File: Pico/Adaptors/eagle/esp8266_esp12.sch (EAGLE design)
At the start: 15 parts, among them J1 JST-2P-SMD-PW-3410050P1

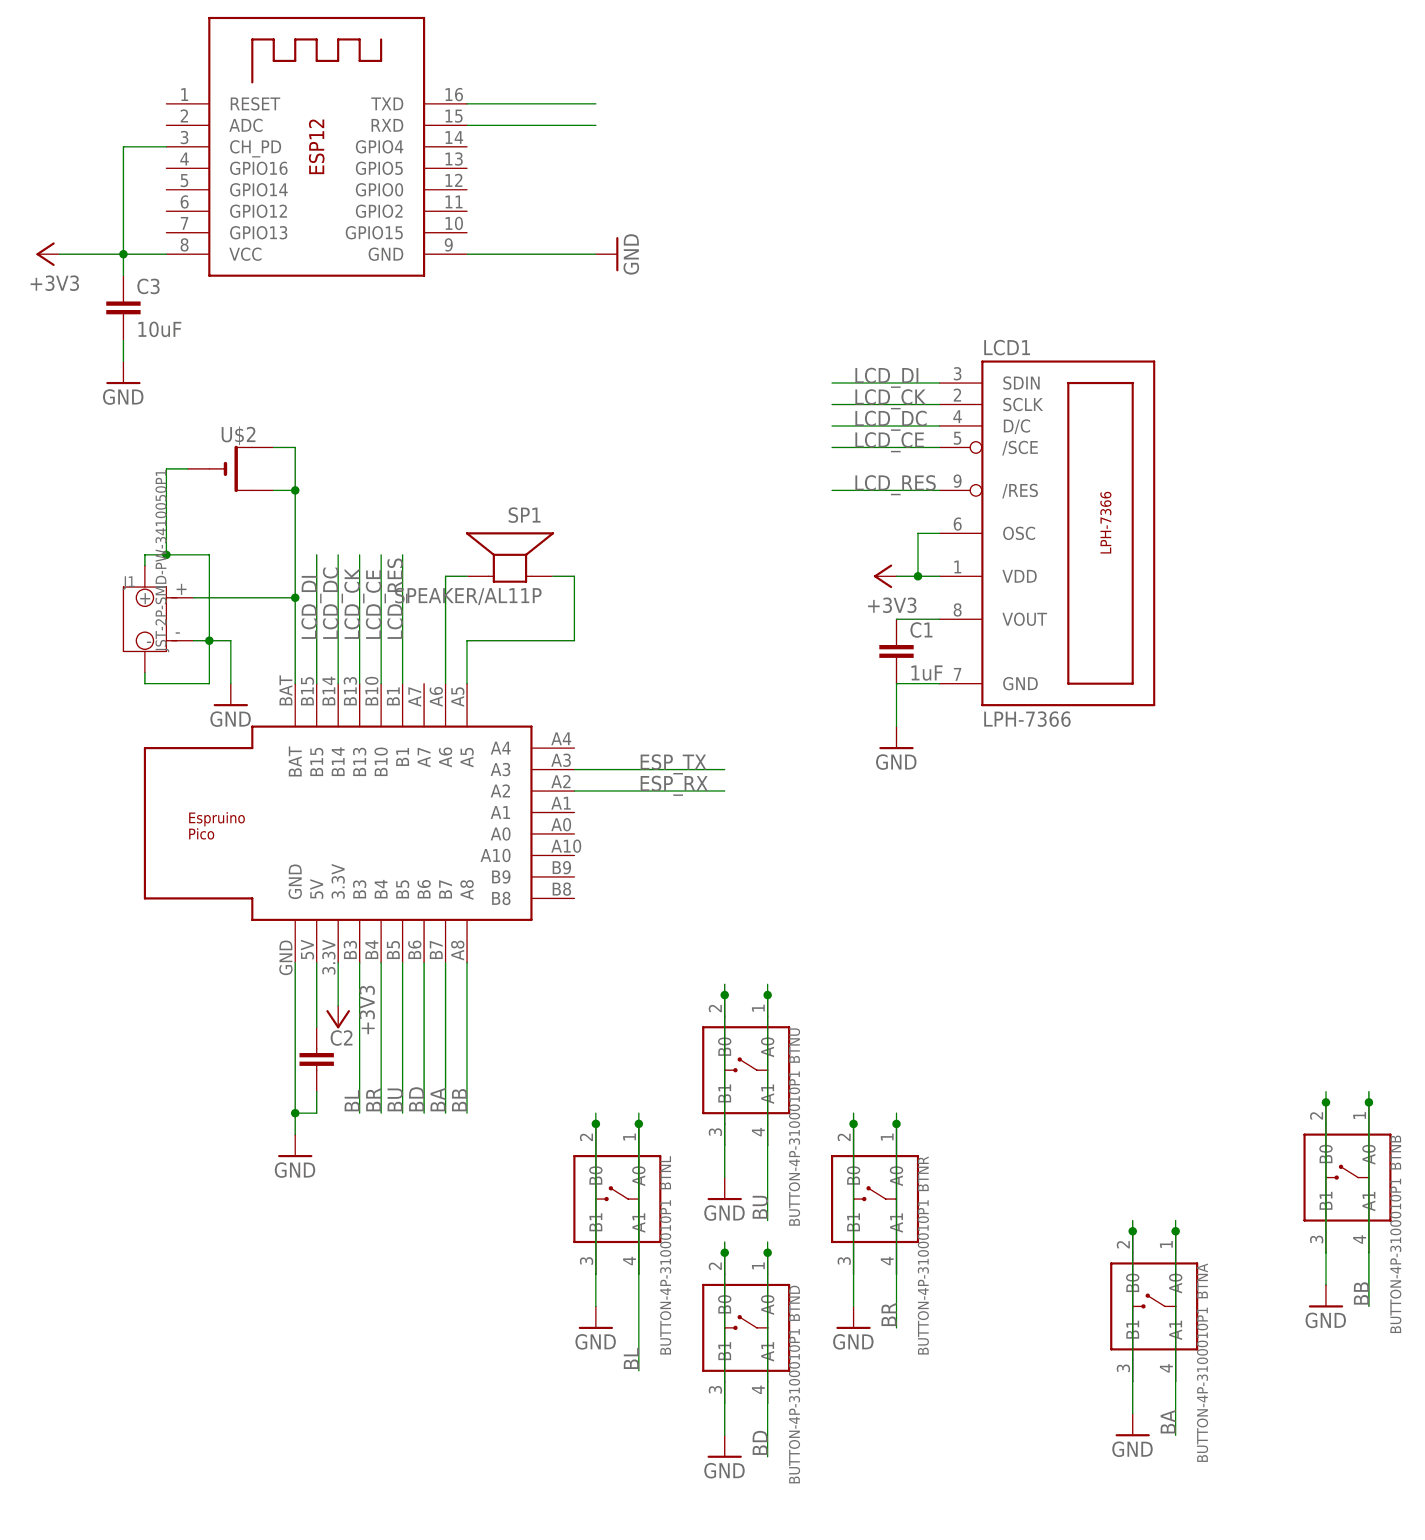
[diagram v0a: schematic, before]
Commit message: added ESP12 shim
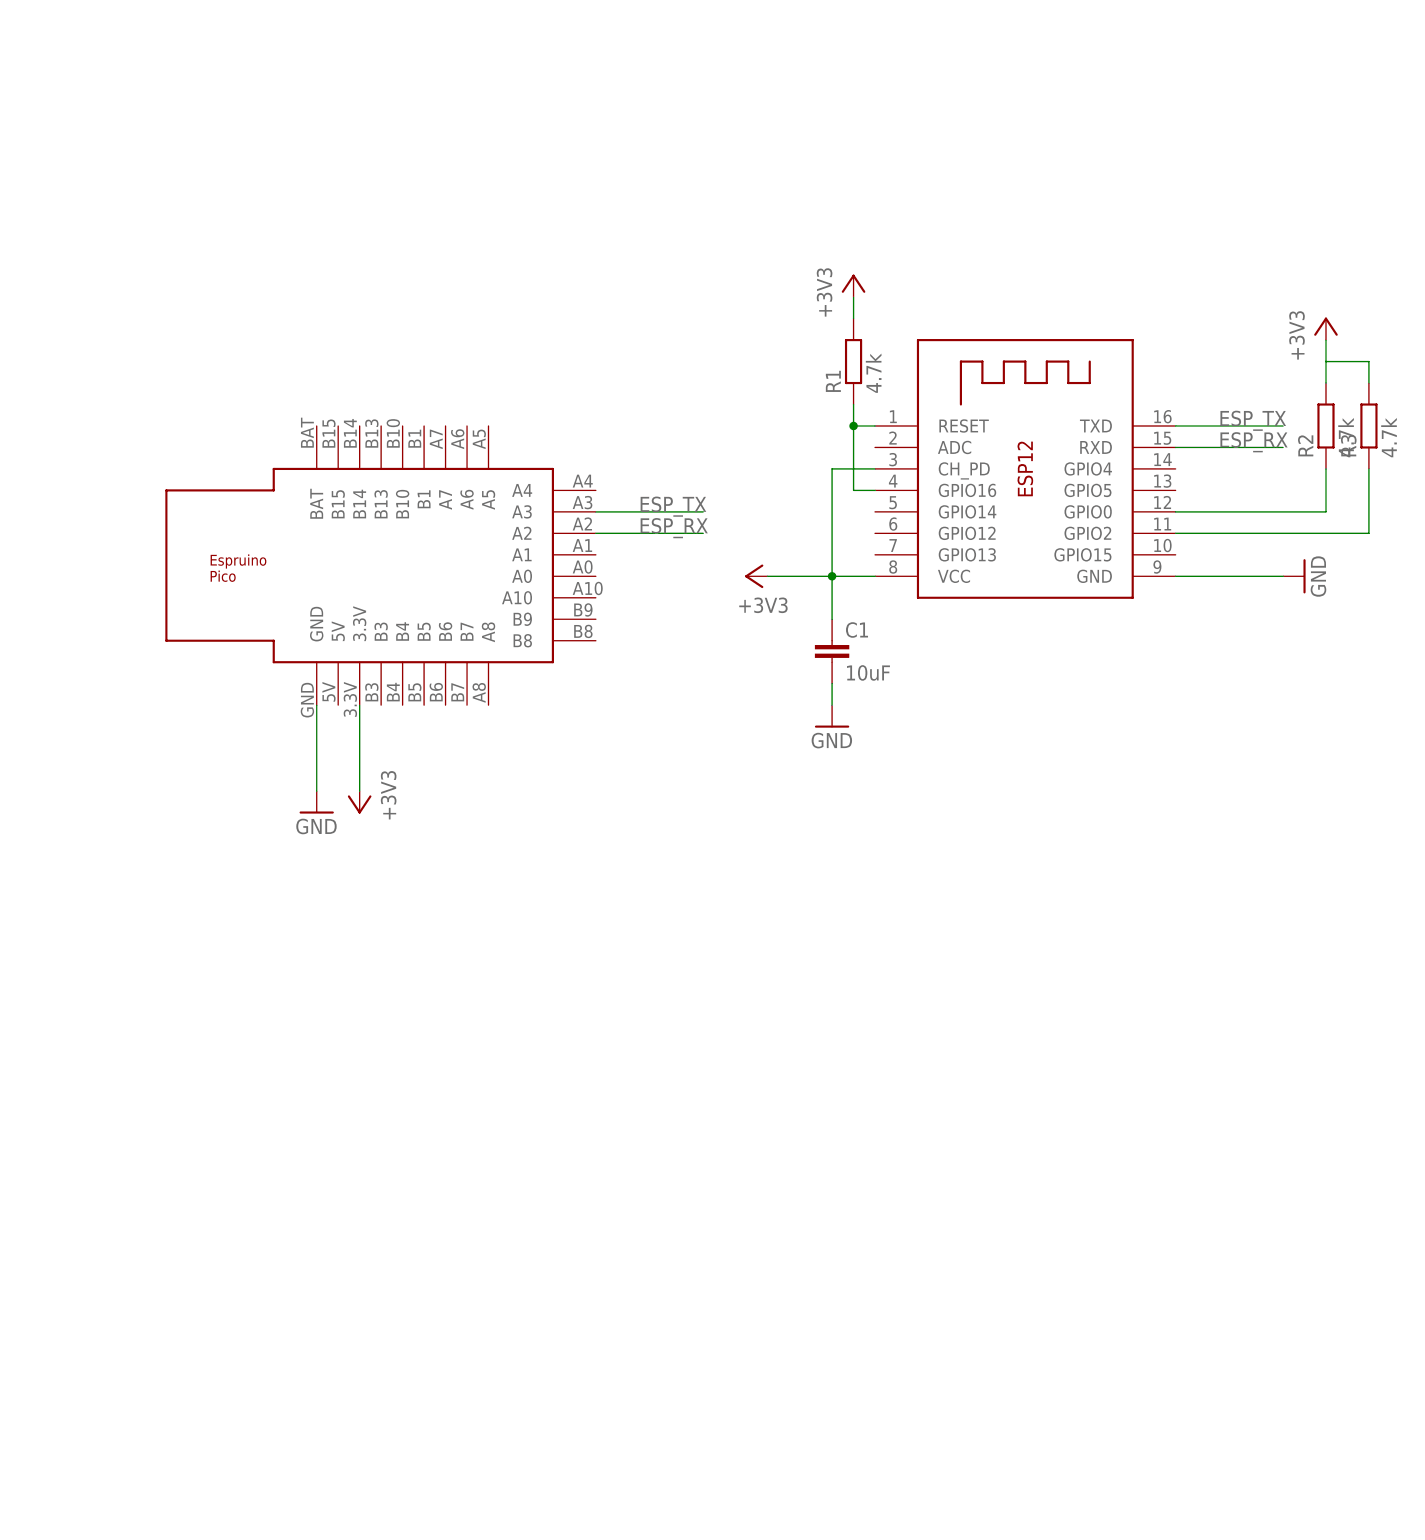
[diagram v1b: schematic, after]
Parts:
- removed BTNA, BTNB, BTND, BTNL, BTNR, BTNU: BUTTON-4P-3100010P1, OPL Eagle Library:BUTTON-4P-3100010P1
- removed C2: (no value), rcl:C-EU050-075X075
- removed C3: 10uF, rcl:C-EUC1206
- removed ESP12: (no value), adafruit:ESP-12
- removed J1: JST-2P-SMD-PW-3410050P1, OPL Eagle Library:JST-2P-SMD-PW-3410050P1
- removed LCD1: LPH-7366, lph-7366:LPH-7366
- removed SP1: SPEAKER/AL11P, adafruit:SPEAKER/AL11P
- removed U$2: (no value), adafruit:CR2032SMT
- added R1, R2, R3: 4.7k, rcl:R-EU_R1206
- added X1: (no value), adafruit:ESP-12
- C1: value 1uF -> 10uF
- U$1: value ESPRUINO_PICO_SMDONLY -> ESPRUINO_PICO_HALFSMD; device espruino_pico:ESPRUINO_PICO_SMDONLY -> espruino_pico:ESPRUINO_PICO_HALFSMD
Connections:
- removed net BA: BTNA.A0, BTNA.A1, U$1.B7
- removed net BB: BTNB.A0, BTNB.A1, U$1.A8
- removed net BD: BTND.A0, BTND.A1, U$1.B6
- removed net BL: BTNL.A0, BTNL.A1, U$1.B3
- removed net BR: BTNR.A0, BTNR.A1, U$1.B4
- removed net BU: BTNU.A0, BTNU.A1, U$1.B5
- removed net LCD_CE: LCD1./SCE, U$1.B10
- removed net LCD_CK: LCD1.SCLK, U$1.B13
- removed net LCD_DC: LCD1.D/C, U$1.B14
- removed net LCD_DI: LCD1.SDIN, U$1.B15
- removed net LCD_RES: LCD1./RES, U$1.B1
- removed net N$3: C2.1, U$1.5V
- removed net N$4: SP1.-, U$1.A6
- removed net N$5: SP1.+, U$1.A5
- new net N$9: R1.1, X1.GPIO16, X1.RESET
- net +3V3: now also C1.1, R1.2, R2.2, R3.2, X1.CH_PD, X1.VCC; no longer C3.1, ESP12.CH_PD, ESP12.VCC, LCD1.OSC, LCD1.VDD
- net ESP_RX: now also X1.RXD; no longer ESP12.RXD
- net ESP_TX: now also X1.TXD; no longer ESP12.TXD
- net GND: now also X1.GND; no longer BTNA.B0, BTNA.B1, BTNB.B0, BTNB.B1, BTND.B0, BTND.B1, BTNL.B0, BTNL.B1, BTNR.B0, BTNR.B1, BTNU.B0, BTNU.B1, C2.2, C3.2, ESP12.GND, J1.-, J1.3, J1.4, LCD1.GND, U$2.-
- net N$1: now also R3.1, X1.GPIO2; no longer C1.1, LCD1.VOUT
- net N$2: now also R2.1, X1.GPIO0; no longer J1.+, U$1.BAT, U$2.+, U$2.+1
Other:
- moved on the sheet: C1
